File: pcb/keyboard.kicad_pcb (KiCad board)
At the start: 4 copper layers, 141 x 98.8 mm, 63 parts, among them J1 USB4510-03-1-A, J2 Battery, J3 Tag-Connect TC2030, Q1 2N7002, SW1 PWR, SW2 Reset, U1 SRV05-4, U2 BQ24075, U3 BT840, Y1 ECS-.327-9-34B-TR

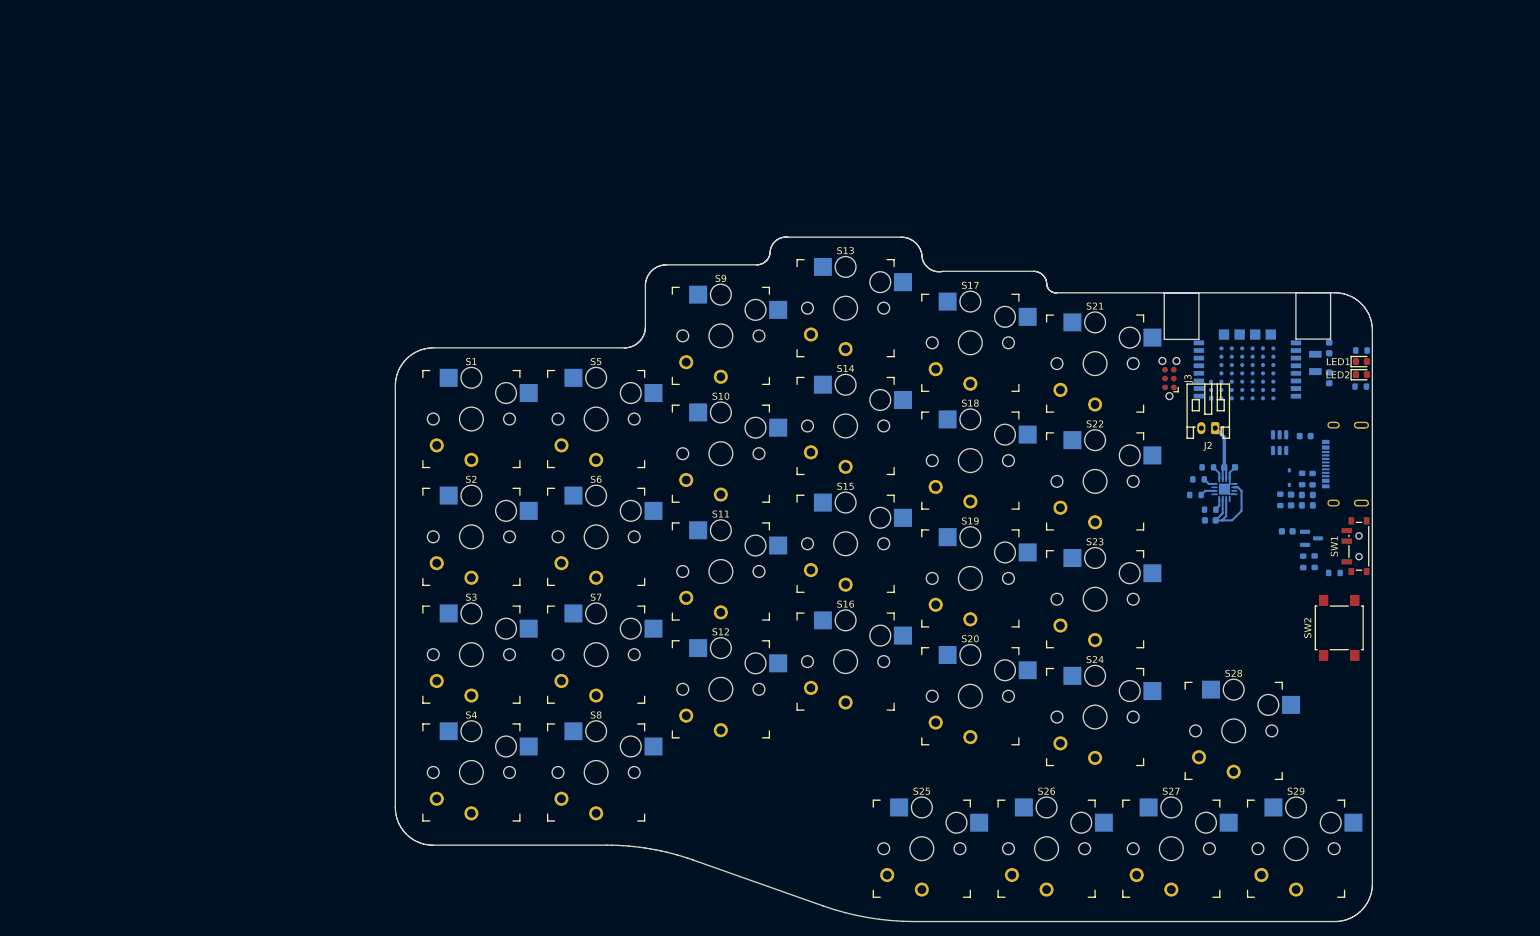
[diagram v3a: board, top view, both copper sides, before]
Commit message: #2 Expand the PCB to accomodate all components
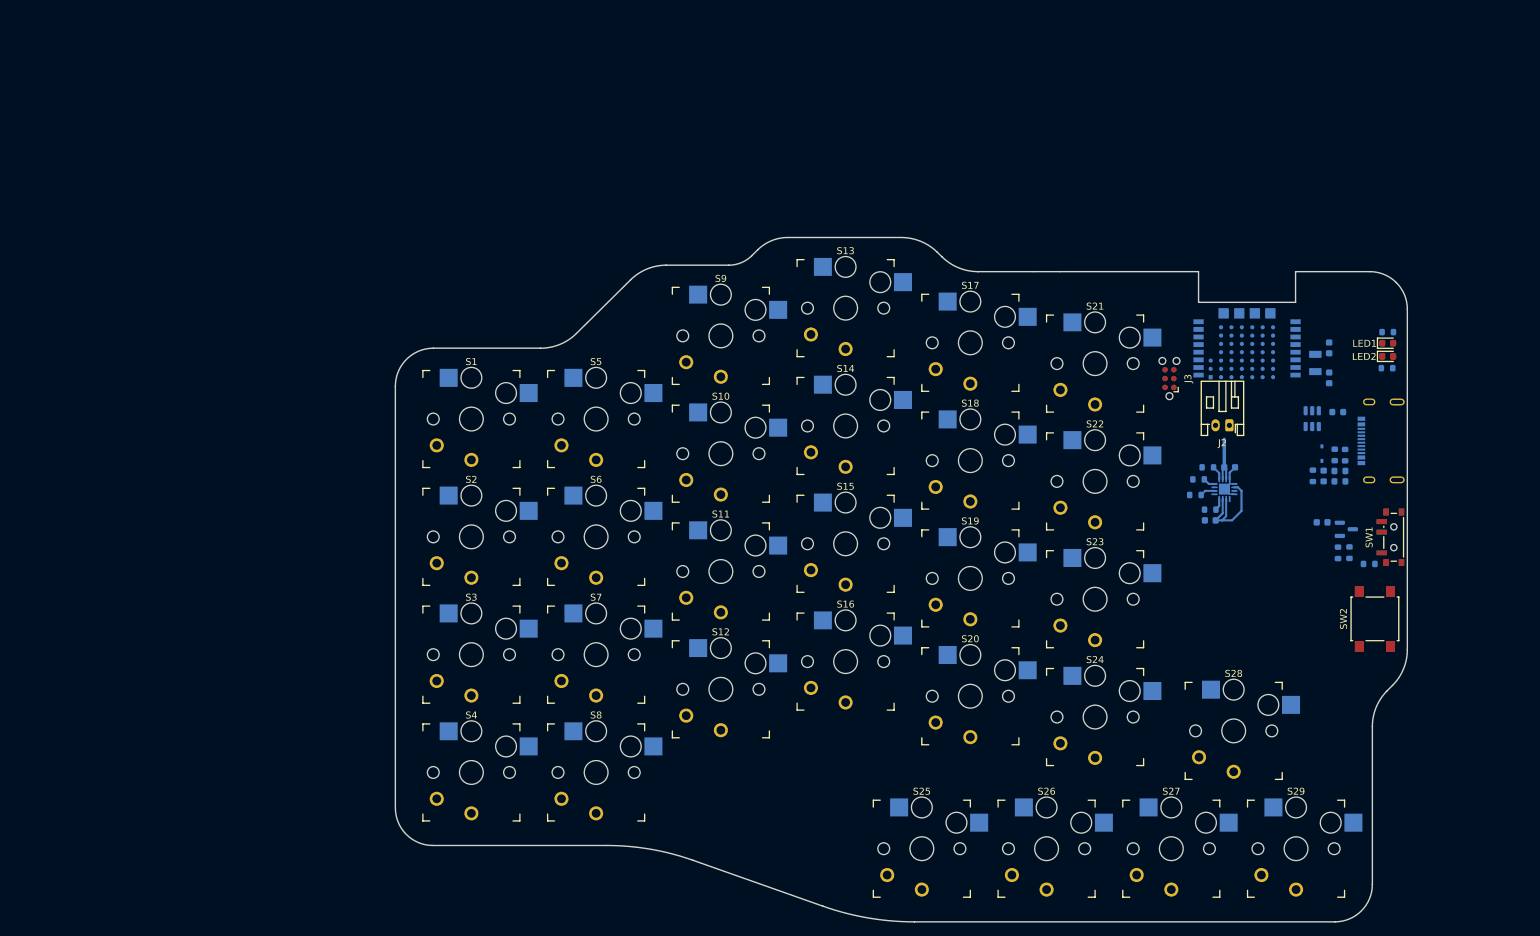
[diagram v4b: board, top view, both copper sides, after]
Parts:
- moved J1 6.14 mm to (276.8, 102.0)
- moved C1 5.84 mm to (267.1, 107.1)
- moved D1 5.84 mm to (266.9, 103.8)
- moved F1 5.84 mm to (269.4, 107.8)
- moved L1 5.84 mm to (269.1, 97.8)
- moved L2 5.84 mm to (269.4, 106.3)
- moved R1 5.84 mm to (265.6, 107.0)
- moved R2 5.84 mm to (270.2, 104.0)
- moved R3 5.84 mm to (268.7, 104.0)
- moved U1 5.84 mm to (265.4, 98.8)
- moved SW2 5.31 mm to (274.5, 127.7)
- moved R10 5.19 mm to (269.2, 118.2)
- moved R11 5.19 mm to (273.7, 119.8)
- moved C2 5.19 mm to (266.9, 113.8)
- moved Q1 5.19 mm to (270.4, 114.8)
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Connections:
- J2 pad 1: +BATT -> GND
- J2 pad 2: GND -> +BATT
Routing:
- net +BATT: track 9.81 -> 7.66 mm
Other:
- board size 141 x 98.8 mm -> 146 x 98.8 mm

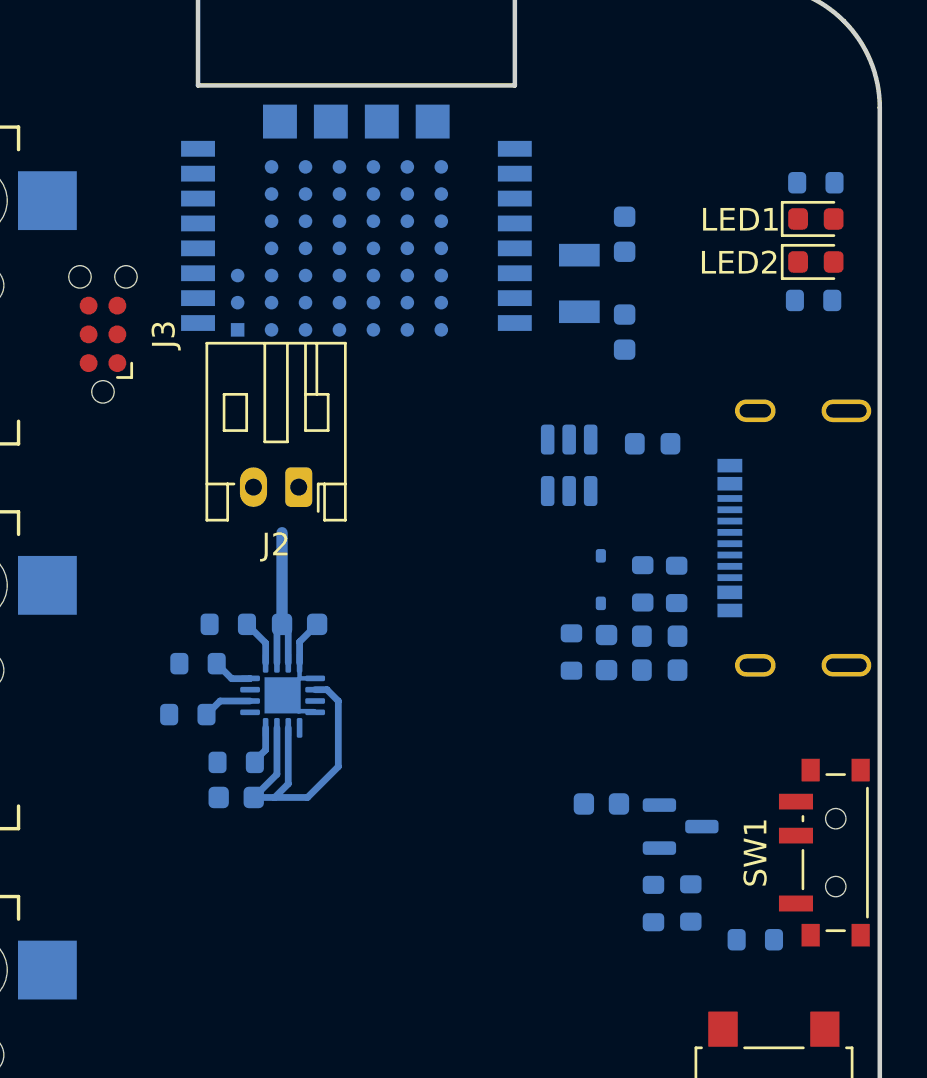
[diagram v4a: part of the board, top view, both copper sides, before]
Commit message: #2 route charging circuit, part 1
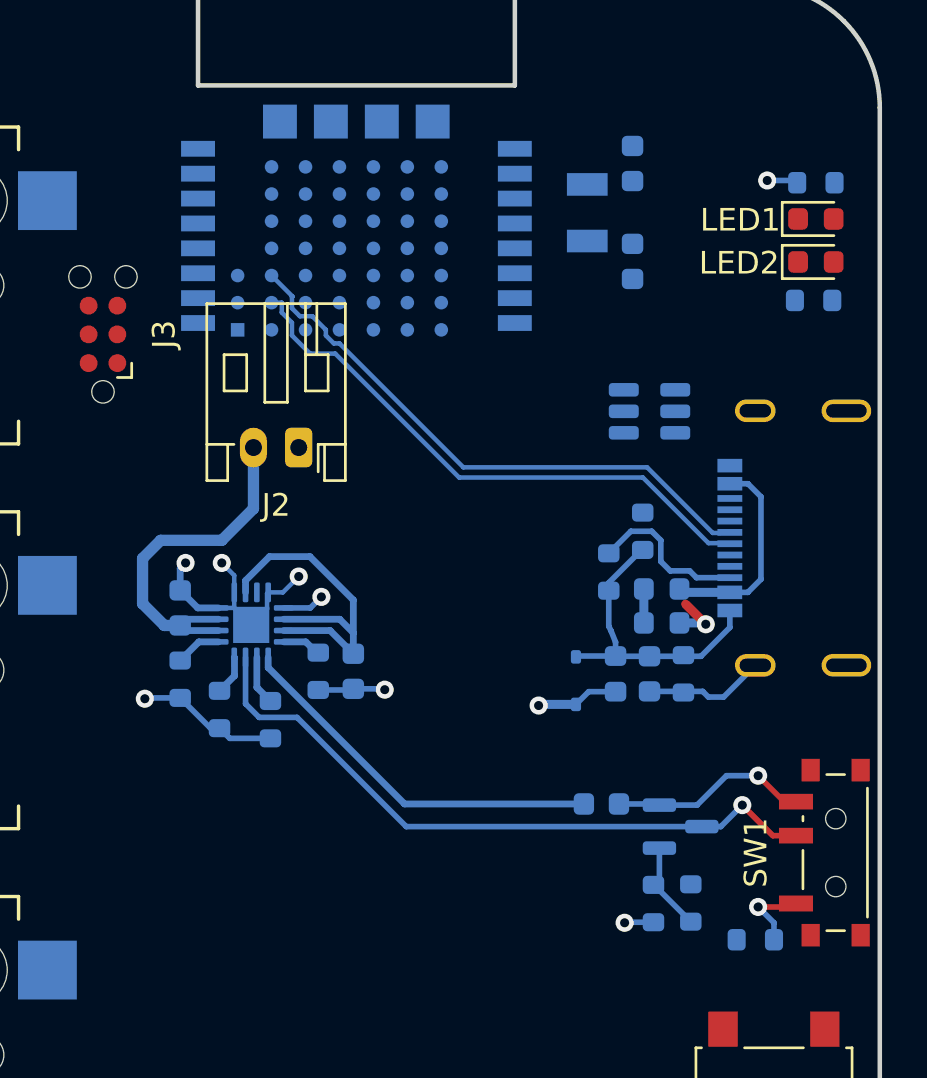
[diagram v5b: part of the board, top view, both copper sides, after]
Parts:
- moved L1 10.3 mm to (267.5, 108.0), turned to -90 degrees
- moved C4 7.61 mm to (255.9, 107.9), turned to -90 degrees
- moved R5 5.42 mm to (254.4, 107.9), turned to -90 degrees
- moved C3 5.32 mm to (248.3, 105.1), turned to 90 degrees
- moved R1 5.04 mm to (270.5, 108.0)
- moved D1 4.60 mm to (265.8, 108.3), turned to -90 degrees
- moved U1 4.28 mm to (269.0, 96.4), turned to 0 degrees
- moved R4 3.66 mm to (252.2, 110.0), turned to -90 degrees
- moved U2 3.41 mm to (251.4, 105.8), turned to 0 degrees
- moved R7 3.22 mm to (248.3, 108.2), turned to -90 degrees
- moved C5 3.14 mm to (268.2, 85.5)
- moved C6 3.14 mm to (268.2, 89.8)
- moved Y1 3.14 mm to (266.2, 87.6)
- moved R2 3.05 mm to (267.2, 103.5)
- moved R3 2.32 mm to (268.7, 101.7), turned to -90 degrees
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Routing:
- net Net-(U2-~{CHG}): track 0.00 -> 31.0 mm, vias 0 -> 2
- net SYSOFF: track 0.00 -> 29.6 mm, vias 0 -> 1
- net GND: track 6.20 -> 33.8 mm, vias 0 -> 8
- net USB-D+: track 0.00 -> 25.5 mm
- net USB-D-: track 0.00 -> 25.2 mm
- net +5V: track 0.00 -> 19.3 mm, vias 0 -> 1
- net GNDPWR: track 0.00 -> 13.5 mm
- net VBUS: track 0.00 -> 9.16 mm
- net +BATT: track 7.66 -> 16.2 mm
- net Net-(J1-CC2): track 0.00 -> 7.15 mm
- net Earth: track 0.00 -> 5.36 mm
- net Net-(Q1-G): track 0.00 -> 4.06 mm
- net Net-(SW1-A): track 0.00 -> 3.47 mm, vias 0 -> 1
- net Net-(F1-Pad1): track 0.00 -> 1.50 mm

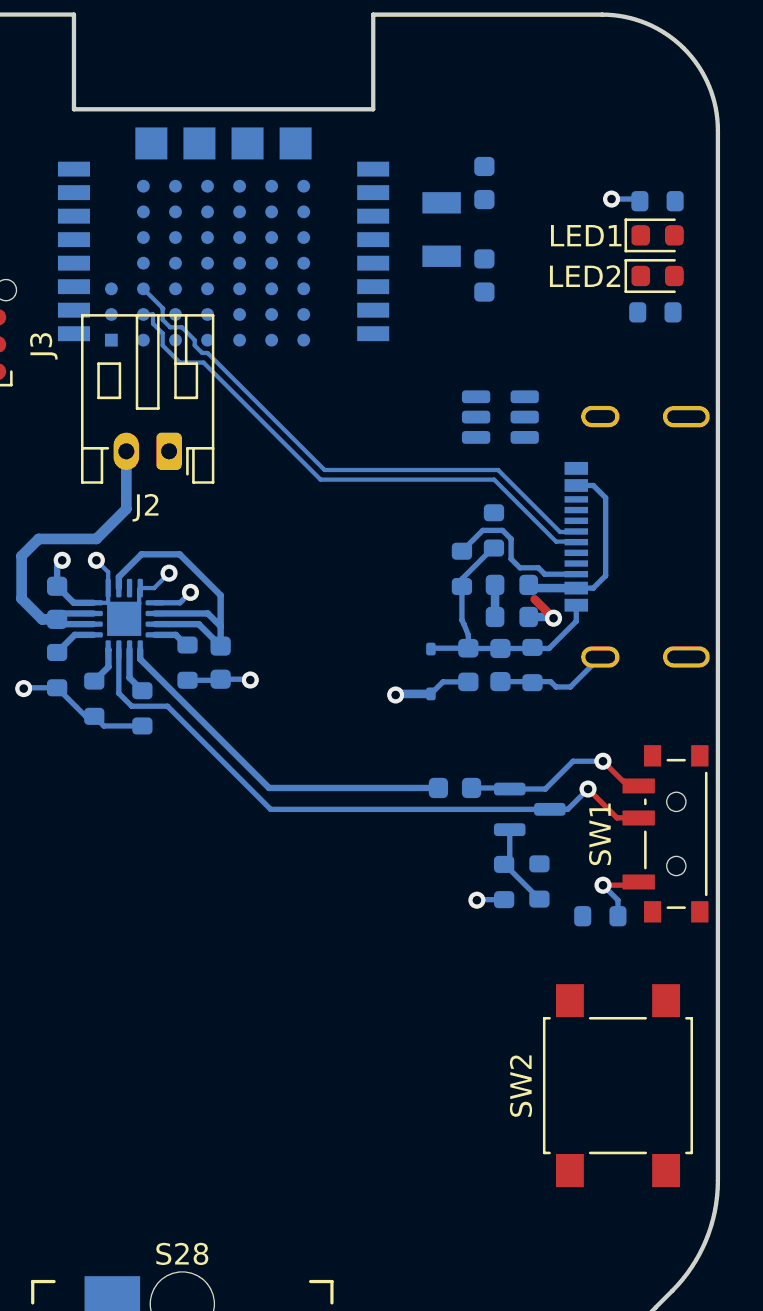
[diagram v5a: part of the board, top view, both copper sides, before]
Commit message: #2 route USB-C connector + diff pair
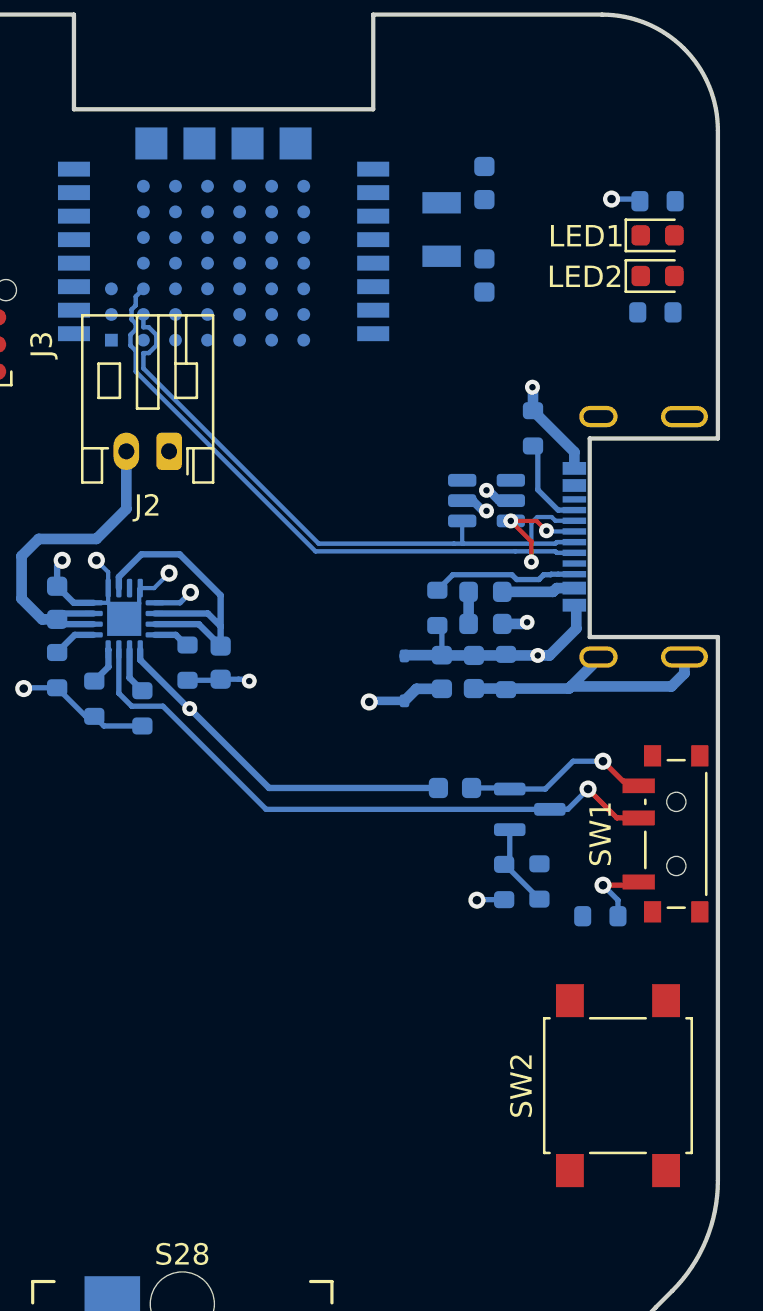
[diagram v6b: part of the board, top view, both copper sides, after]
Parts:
- moved R3 5.11 mm to (270.5, 96.9)
- moved U1 3.96 mm to (268.4, 100.3)
- moved R2 2.16 mm to (266.1, 105.3)
- moved C1 1.28 mm to (267.8, 108.3)
- moved D1 1.28 mm to (264.5, 108.6)
- moved F1 1.28 mm to (268.3, 106.1)
- moved L1 1.28 mm to (266.3, 108.3)
- moved L2 1.28 mm to (268.3, 104.6)
- moved R1 1.28 mm to (269.3, 108.3)
- moved J1 0.09 mm to (276.7, 102.0)
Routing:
- net +5V: track 19.3 -> 44.6 mm, vias 1 -> 3
- net Earth: track 5.36 -> 29.6 mm
- net GNDPWR: track 13.5 -> 29.4 mm, vias 0 -> 2
- net USB-D+: track 25.5 -> 34.6 mm, vias 0 -> 3
- net USB-D-: track 25.2 -> 31.2 mm
- net VBUS: track 9.16 -> 3.69 mm
- net Net-(J1-CC1): track 0.00 -> 4.25 mm
- net GND: track 33.8 -> 35.1 mm, vias 8 -> 9
- added copper zone on In2.Cu, net GND
- removed copper zone on In1.Cu, net GND
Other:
- outline, holes or cut-outs redrawn
